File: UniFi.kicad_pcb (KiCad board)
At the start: 2 copper layers, 120.2 x 100.1 mm, 67 parts, among them J1 OLED, J2 MJ-4PP-9 TRRS, SW1 SW_PUSH-MX_W_LED, SW10 SW_PUSH-MX_W_LED, SW11 SW_PUSH-MX_W_LED, SW12 SW_PUSH-MX_W_LED, SW13 SW_PUSH-MX_W_LED, SW14 SW_PUSH-MX_W_LED, SW15 SW_PUSH-MX_W_LED, SW16 SW_PUSH-MX_W_LED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

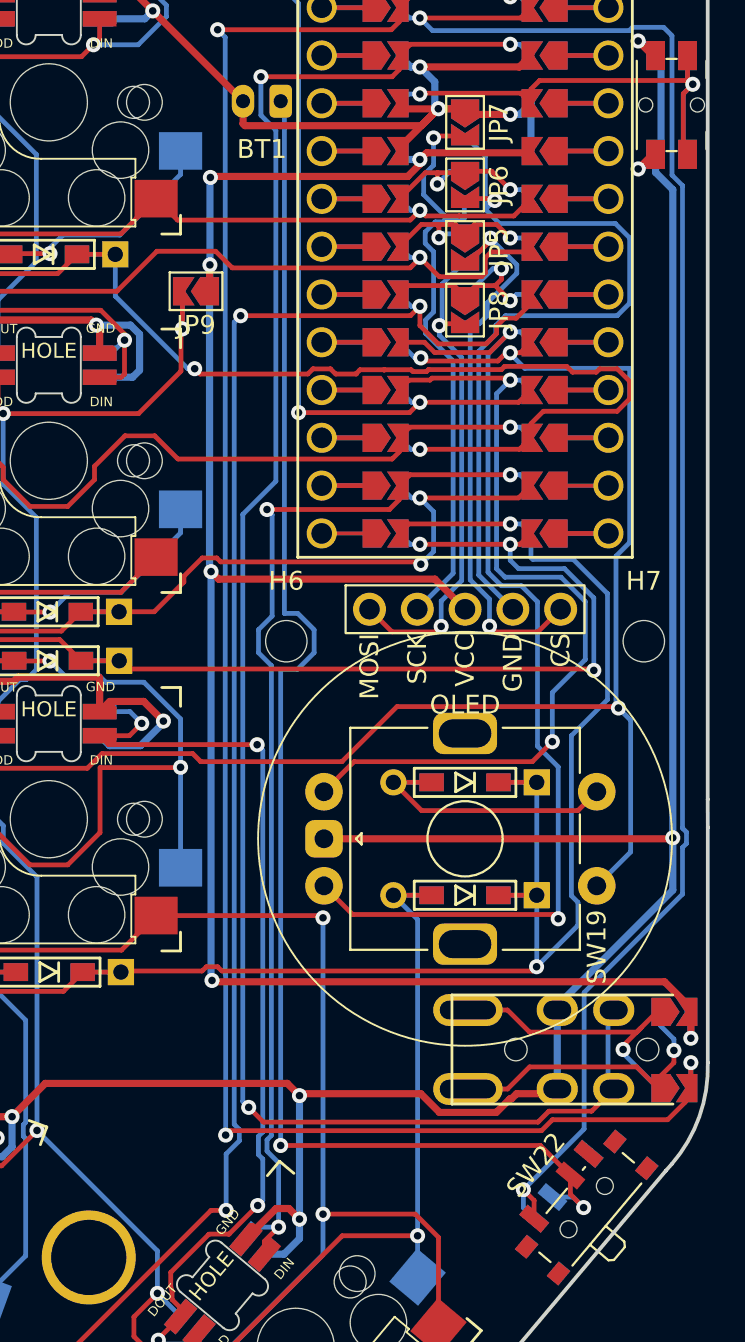
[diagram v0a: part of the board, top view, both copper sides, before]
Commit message: Updated pins
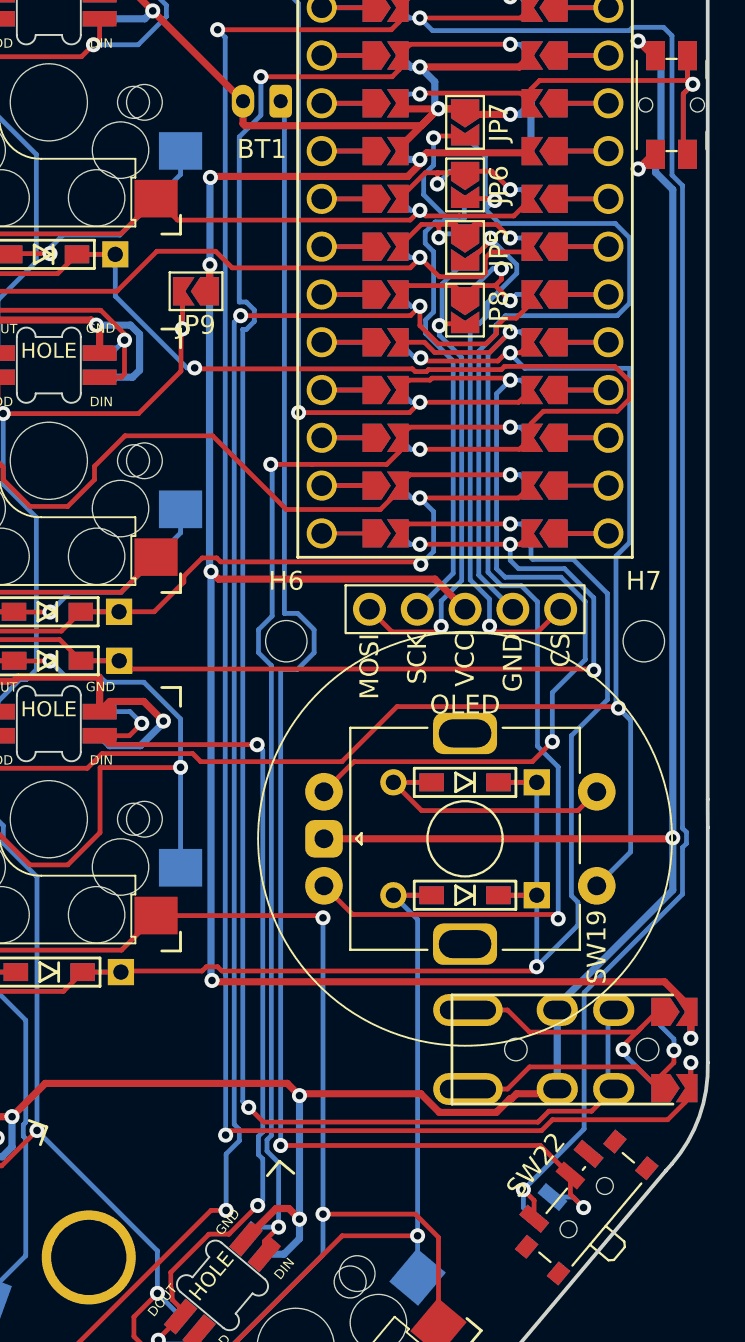
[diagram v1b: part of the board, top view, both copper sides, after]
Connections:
- U1 pad 10: AUDIO -> LED
- U1 pad 11: LED -> AUDIO
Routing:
- net LED: track 58.4 -> 60.6 mm
- net AUDIO: track 97.0 -> 97.9 mm
- net ROW1: track 148.1 -> 147.5 mm

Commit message: Added References
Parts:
- renumbered SW22 to Power, SW23 to Ppwer
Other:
- board text added: "Buzzer"
- board text added: "JLCJLCJLC"
- board text added: "OLED"
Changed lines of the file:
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@@
     (property "ki_keywords" "switch single-pole double-throw spdt ON-ON")
     (attr smd)
-    (fp_text reference "SW22" (at 0 -3.2 50) (layer "F.SilkS")
+    (fp_text reference "Power" (at 0 -3.2 50) (layer "F.SilkS")
         (effects (font (size 1 1) (thickness 0.15)))
     )
@@
     (property "ki_keywords" "mounting hole")
     (attr exclude_from_pos_files)
-    (fp_text reference "H7" (at 0 -3.2) (layer "F.SilkS")
+    (fp_text reference "H7" (at 0 -3.2) (layer "F.SilkS") hide
         (effects (font (size 1 1) (thickness 0.15)))
     )
@@
         (effects (font (size 1 1) (thickness 0.15)))
     )
-    (fp_text user "TRRS" (at 0 5.08) (layer "F.Fab")
+    (fp_text user "TRRS" (at 0 5.2 unlocked) (layer "B.SilkS")
+        (effects (font (size 1 1) (thickness 0.15)) (justify mirror))
+    )
+    (fp_text user "TRRS" (at 0 5.08) (layer "F.SilkS")
         (effects (font (size 1 1) (thickness 0.15)))
     )
@@
         (effects (font (size 1 1) (thickness 0.15)))
     )
-    (fp_text user "${REFERENCE}" (at 0 0 90) (layer "F.Fab")
+    (fp_text user "RST" (at 0 0 90) (layer "F.SilkS")
         (effects (font (size 1 1) (thickness 0.15)))
     )
@@
         (effects (font (size 1 1) (thickness 0.15)))
     )
-    (fp_text value "OLED" (at 0 21.59 unlocked) (layer "F.SilkS")
+    (fp_text value "OLED" (at 0 19 unlocked) (layer "F.SilkS")
         (effects (font (size 1 1) (thickness 0.15)))
     )
-    (fp_text user "CS" (at 5.08 17.78 90 unlocked) (layer "F.SilkS")
+    (fp_text user "CS" (at 5.08 17.78 90 unlocked) (layer "F.SilkS") hide
         (effects (font (size 1 1) (thickness 0.15)) (justify right))
     )
-    (fp_text user "MOSI" (at -5.08 17.78 90 unlocked) (layer "F.SilkS")
+    (fp_text user "MOSI" (at -5.08 17.78 90 unlocked) (layer "F.SilkS") hide
         (effects (font (size 1 1) (thickness 0.15)) (justify right))
     )
-    (fp_text user "SCK" (at -2.54 17.78 90 unlocked) (layer "F.SilkS")
+    (fp_text user "SCK" (at -2.54 17.78 90 unlocked) (layer "F.SilkS") hide
         (effects (font (size 1 1) (thickness 0.15)) (justify right))
     )
-    (fp_text user "VCC" (at 0 17.78 90 unlocked) (layer "F.SilkS")
+    (fp_text user "VCC" (at 0 17.78 90 unlocked) (layer "F.SilkS") hide
         (effects (font (size 1 1) (thickness 0.15)) (justify right))
     )
-    (fp_text user "GND" (at 2.54 17.78 90 unlocked) (layer "F.SilkS")
+    (fp_text user "GND" (at 2.54 17.78 90 unlocked) (layer "F.SilkS") hide
         (effects (font (size 1 1) (thickness 0.15)) (justify right))
     )
@@
         (effects (font (size 1 1) (thickness 0.15)))
     )
+    (fp_rect (start 6.35 15.24) (end -6.35 17.78)
+      (stroke (width 0.12) (type solid)) (fill none) (layer "B.SilkS"))
     (fp_rect (start -6.35 15.24) (end 6.35 17.78)
       (stroke (width 0.12) (type solid)) (fill none) (layer "F.SilkS"))
@@
     (property "ki_keywords" "quartz resonator ceramic")
     (attr smd)
-    (fp_text reference "BZ1" (at 0 5.5) (layer "F.SilkS")
+    (fp_text reference "BZ1" (at 0 5.5) (layer "F.SilkS") hide
         (effects (font (size 1 1) (thickness 0.15)))
     )
-    (fp_text value "Buzzer" (at 0 -5.5) (layer "F.Fab")
+    (fp_text value "Buzzer" (at 3 -5.5) (layer "F.SilkS")
         (effects (font (size 1 1) (thickness 0.15)))
     )
-    (fp_text user "${REFERENCE}" (at 0 0) (layer "F.Fab")
+    (fp_text user "${REFERENCE}" (at 0 0) (layer "F.Fab") hide
         (effects (font (size 1 1) (thickness 0.15)))
     )
@@
     (property "ki_keywords" "mounting hole")
     (attr exclude_from_pos_files)
-    (fp_text reference "H6" (at 0 -3.2) (layer "F.SilkS")
+    (fp_text reference "H6" (at 0 -3.2) (layer "F.SilkS") hide
         (effects (font (size 1 1) (thickness 0.15)))
     )
@@
     (property "ki_keywords" "rotary switch encoder switch push button")
     (attr through_hole)
-    (fp_text reference "SW19" (at 5.75 -7 90) (layer "F.SilkS")
+    (fp_text reference "SW19" (at 5.75 -7 90) (layer "F.SilkS") hide
         (effects (font (size 1 1) (thickness 0.15)))
     )
@@
         (effects (font (size 1 1) (thickness 0.15)))
     )
-    (fp_text user "${REFERENCE}" (at 0 0 90) (layer "F.Fab")
+    (fp_text user "Encoder" (at 0 0 unlocked) (layer "B.SilkS")
+        (effects (font (size 1 1) (thickness 0.15)) (justify mirror))
+    )
+    (fp_text user "Encoder" (at 0 0) (layer "F.SilkS")
         (effects (font (size 1 1) (thickness 0.15)))
     )
-    (fp_line (start -5.9 -6.1) (end -3.5 -6.1)
-      (stroke (width 0.12) (type solid)) (layer "F.SilkS"))
-    (fp_line (start -5.9 -2) (end -5.9 -6.1)
-      (stroke (width 0.12) (type solid)) (layer "F.SilkS"))
-    (fp_line (start -5.9 2) (end -5.9 6.1)
-      (stroke (width 0.12) (type solid)) (layer "F.SilkS"))
-    (fp_line (start -5.9 6.1) (end 5.9 6.1)
-      (stroke (width 0.12) (type solid)) (layer "F.SilkS"))
-    (fp_line (start -1.3 -6.1) (end 1.3 -6.1)
-      (stroke (width 0.12) (type solid)) (layer "F.SilkS"))
-    (fp_line (start -0.3 5.5) (end 0.3 5.5)
-      (stroke (width 0.12) (type solid)) (layer "F.SilkS"))
-    (fp_line (start 0 5.8) (end -0.3 5.5)
-      (stroke (width 0.12) (type solid)) (layer "F.SilkS"))
-    (fp_line (start 0.3 5.5) (end 0 5.8)
-      (stroke (width 0.12) (type solid)) (layer "F.SilkS"))
-    (fp_line (start 3.5 -6.1) (end 5.9 -6.1)
-      (stroke (width 0.12) (type solid)) (layer "F.SilkS"))
-    (fp_line (start 5.9 -6.1) (end 5.9 -2)
-      (stroke (width 0.12) (type solid)) (layer "F.SilkS"))
-    (fp_line (start 5.9 2) (end 5.9 6.1)
-      (stroke (width 0.12) (type solid)) (layer "F.SilkS"))
-    (fp_circle (center 0 0) (end 0 -2)
-      (stroke (width 0.12) (type solid)) (fill none) (layer "F.SilkS"))
-    (fp_circle (center 0 0) (end 11 0)
-      (stroke (width 0.1) (type default)) (fill none) (layer "F.SilkS"))
     (fp_line (start -7.1 9) (end -7.1 -8.5)
       (stroke (width 0.05) (type solid)) (layer "F.CrtYd"))
@@
     (fp_line (start 5.8 6) (end -4.7 6)
       (stroke (width 0.12) (type solid)) (layer "F.Fab"))
-    (pad "A" thru_hole circle (at -2.5 7.5) (size 2 2) (drill 1) (layers "*.Cu" "B.Mask")
+    (pad "A" thru_hole circle (at -2.5 7.5) (size 2 2) (drill 1) (layers "*.Cu" "*.Mask")
       (net 39 "ECA") (pinfunction "A") (pintype "passive"))
-    (pad "B" thru_hole circle (at 2.5 7.5) (size 2 2) (drill 1) (layers "*.Cu" "B.Mask")
+    (pad "B" thru_hole circle (at 2.5 7.5) (size 2 2) (drill 1) (layers "*.Cu" "*.Mask")
       (net 40 "ECB") (pinfunction "B") (pintype "passive"))
-    (pad "C" thru_hole roundrect (at 0 7.5) (size 2 2) (drill 1) (layers "*.Cu" "B.Mask") (roundrect_rratio 0.25)
+    (pad "C" thru_hole roundrect (at 0 7.5) (size 2 2) (drill 1) (layers "*.Cu" "*.Mask") (roundrect_rratio 0.25)
       (net 2 "GND") (pinfunction "C") (pintype "passive"))
     (pad "MP" thru_hole roundrect (at -5.6 0) (size 3.4 2.2) (drill oval 2.8 1.5) (layers "*.Cu" "B.Mask") (roundrect_rratio 0.25))
     (pad "MP" thru_hole roundrect (at 5.6 0) (size 3.4 2.2) (drill oval 2.8 1.5) (layers "*.Cu" "B.Mask") (roundrect_rratio 0.25))
-    (pad "S1" thru_hole circle (at 2.5 -7) (size 2 2) (drill 1) (layers "*.Cu" "B.Mask")
+    (pad "S1" thru_hole circle (at 2.5 -7) (size 2 2) (drill 1) (layers "*.Cu" "*.Mask")
       (net 20 "COL2") (pinfunction "S1") (pintype "passive"))
-    (pad "S2" thru_hole circle (at -2.5 -7) (size 2 2) (drill 1) (layers "*.Cu" "B.Mask")
+    (pad "S2" thru_hole circle (at -2.5 -7) (size 2 2) (drill 1) (layers "*.Cu" "*.Mask")
       (net 7 "ECR") (pinfunction "S2") (pintype "passive"))
     (model "${KICAD7_3RD_PARTY}/3dmodels/com_github_ebastler_marbastlib/ROT_EC11E.step"
@@
     (property "ki_keywords" "switch single-pole double-throw spdt ON-ON")
     (attr smd)
-    (fp_text reference "SW23" (at 0 3.2 50) (layer "B.SilkS")
+    (fp_text reference "Ppwer" (at 0 3.2 50) (layer "B.SilkS")
         (effects (font (size 1 1) (thickness 0.15)) (justify mirror))
     )
@@
     (property "ki_keywords" "Switch")
     (attr smd)
-    (fp_text reference "SW21" (at 0 4.5 270) (layer "B.SilkS")
+    (fp_text reference "SW21" (at 0 4.5 270) (layer "B.SilkS") hide
         (effects (font (size 1 1) (thickness 0.15)) (justify mirror))
     )
@@
         (effects (font (size 1 1) (thickness 0.15)) (justify mirror))
     )
-    (fp_text user "${REFERENCE}" (at 0 0 270) (layer "B.Fab")
+    (fp_text user "RST" (at 0 0 90) (layer "B.SilkS")
         (effects (font (size 1 1) (thickness 0.15)) (justify mirror))
     )
@@
   (gr_arc (start 182.949289 96.7) (mid 181.341561 99.069037) (end 178.546228 98.449973)
     (stroke (width 0.1) (type default)) (layer "User.9"))
+  (gr_text "JLCJLCJLC" (at 170.9 86.1 -90) (layer "B.SilkS")
+    (effects (font (size 1 1) (thickness 0.15)) (justify mirror))
+  )
+  (gr_text "OLED" (at 171 96.8) (layer "B.SilkS")
+    (effects (font (size 1 1) (thickness 0.15)) (justify mirror))
+  )
+  (gr_text "Buzzer" (at 108.1 114.9) (layer "B.SilkS")
+    (effects (font (size 1 1) (thickness 0.15)) (justify mirror))
+  )
   (gr_text "github.com/Nisha51/Unifi" (at 174.75 131.25 50) (layer "B.SilkS")
     (effects (font (size 1 1) (thickness 0.15)) (justify left bottom mirror))
@@
     (effects (font (size 1 1) (thickness 0.15)) (justify left bottom))
   )
+  (gr_text "JLCJLCJLC" (at 171 86.1 90) (layer "F.SilkS")
+    (effects (font (size 1 1) (thickness 0.15)))
+  )
   (segment (start 175.95 80.11) (end 178.62 80.11) (width 0.254) (layer "F.Cu") (net 0))

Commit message: Update UniFi.kicad_pcb
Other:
- board text removed: "JLCJLCJLC"
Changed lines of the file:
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@@
   (gr_arc (start 182.949289 96.7) (mid 181.341561 99.069037) (end 178.546228 98.449973)
     (stroke (width 0.1) (type default)) (layer "User.9"))
-  (gr_text "JLCJLCJLC" (at 170.9 86.1 -90) (layer "B.SilkS")
-    (effects (font (size 1 1) (thickness 0.15)) (justify mirror))
-  )
   (gr_text "OLED" (at 171 96.8) (layer "B.SilkS")
     (effects (font (size 1 1) (thickness 0.15)) (justify mirror))
@@
     (effects (font (size 1 1) (thickness 0.15)) (justify left bottom))
   )
-  (gr_text "JLCJLCJLC" (at 171 86.1 90) (layer "F.SilkS")
-    (effects (font (size 1 1) (thickness 0.15)))
-  )
   (segment (start 175.95 80.11) (end 178.62 80.11) (width 0.254) (layer "F.Cu") (net 0))
